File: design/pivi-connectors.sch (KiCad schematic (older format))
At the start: 13 parts, among them P1 Recom_Power_RAC10-05SC/277, P3 CONN_01X05, P4 CONN_01X02, P6 CONN_01X02, P7 CONN_01X05, P8 CONN_01X02, P9 CONN_02X20

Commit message: Moving to PIVI 2.0, added circuits for current clamps
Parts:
- removed P3, P7: CONN_01X05, LESS:CONN-TERM-BLK-5POS-PHOENIX, symbol CONN_01X05
- removed P8: CONN_01X02, LESS:CONN-TERM-BLK-2POS-PHOENIX, symbol CONN_01X02
- added D?: LED_RGB, symbol LED_RGB
- added R? (x3): 270, symbol R
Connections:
- net labels added: CT1_1, CT1_2, CT1_DETECTOR, CT2_1, CT2_2, CT2_DETECTOR, CT3_1, CT3_2, CT3_DETECTOR, CT4_1, CT4_2, CT4_DETECTOR, CT5_1, CT5_2, CT5_DETECTOR, CT6_1, CT6_2, CT6_DETECTOR, GPIO-12, GPIO-18, GPIO-23, GPIO-24, GPIO-25, Neutral_Line, Phase_In
- net labels removed: Neutral1_In, Neutral1_Out, Phase1_In, Phase1_Out, Phase2_In, Phase2_Out, Phase3_In, Phase3_Out, Phase4_In, Phase4_Out, Phase5_In, Phase5_Out, Phase6_In, Phase6_Out
- wire segments 48 -> 72
- no-connect marks 26 -> 21
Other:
- note added: "Audio Jack 3.5 mm female connector\n"
- note added: "Clamp audio connections for SCT-013-000"
- note added: "SJ-3506-SMT"
- note added: "The GPIO pins can draw 50mA safely, distributed\nacross all the pins; an individual GPIO pin can \nonly safely draw 16mA. \n\nhttps://www.raspberrypi.org/documentation/hardw"
- note added: "This connector must meet the following requirements:\n* Internal switch : Avoids noise in pins when the clamp is unplugged.\n* Shielded : Increase endurance, stregth and avoid noise."
- note removed: "277-9761-ND"
- note removed: "Power line output.\nTo load."
- moved on the sheet: C21, D1, JP1, L15, L16, P1, P4, P6, P9, R9

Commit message: Fixing connection errors
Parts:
- gave numbers to parts that had none: 4
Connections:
- net Phase_In renamed Phase_Line
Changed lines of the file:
@@
 Board power Supply Connections
 Text HLabel 7475 5230 2    60   Output ~ 0
-Phase_In
+Phase_Line
 Text HLabel 7475 5330 2    60   Output ~ 0
 Neutral_Line
@@
 GPIO-23
 $Comp
-L LED_RGB D?
+L LED_RGB D2
 U 1 1 55BA51D0
 P 8540 2390
-F 0 "D?" H 8540 2840 50  0000 C CNN
+F 0 "D2" H 8540 2840 50  0000 C CNN
 F 1 "LED_RGB" H 8540 2740 50  0000 C CNN
 F 2 "" H 8540 2340 60  0000 C CNN
@@
 $EndComp
 $Comp
-L R R?
+L R R36
 U 1 1 55BA6452
 P 9040 2190
-F 0 "R?" V 9120 2190 50  0000 C CNN
+F 0 "R36" V 9120 2190 50  0000 C CNN
 F 1 "270" V 9040 2190 50  0000 C CNN
 F 2 "" V 8970 2190 30  0000 C CNN
@@
 $EndComp
 $Comp
-L R R?
+L R R37
 U 1 1 55BA6613
 P 9040 2390
-F 0 "R?" V 9120 2390 50  0000 C CNN
+F 0 "R37" V 9120 2390 50  0000 C CNN
 F 1 "270" V 9040 2390 50  0000 C CNN
 F 2 "" V 8970 2390 30  0000 C CNN
@@
 $EndComp
 $Comp
-L R R?
+L R R38
 U 1 1 55BA674E
 P 9040 2590
-F 0 "R?" V 9120 2590 50  0000 C CNN
+F 0 "R38" V 9120 2590 50  0000 C CNN
 F 1 "270" V 9040 2590 50  0000 C CNN
 F 2 "" V 8970 2590 30  0000 C CNN
@@
 	9440 2190 9440 2915
 $Comp
-L GND #PWR?
+L GND #PWR033
 U 1 1 55BA8447
 P 9440 2915
-F 0 "#PWR?" H 9440 2665 60  0001 C CNN
+F 0 "#PWR033" H 9440 2665 60  0001 C CNN
 F 1 "GND" H 9440 2765 60  0000 C CNN
 F 2 "" H 9440 2915 60  0000 C CNN

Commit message: Agrego los dos circuitos extra para medir tension
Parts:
- D2: footprint (none) -> LEDs:LED_RGB_PLLC-6
- R36, R37, R38: footprint (none) -> Resistors_SMD:R_0603
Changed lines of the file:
@@
 LIBS:memory
 LIBS:xilinx
-LIBS:special
 LIBS:microcontrollers
 LIBS:dsp
@@
 $Descr A4 11693 8268
 encoding utf-8
-Sheet 3 18
+Sheet 3 20
 Title "PIVI"
 Date "Mon 27 Jul 2015"
@@
 F 0 "D2" H 8540 2840 50  0000 C CNN
 F 1 "LED_RGB" H 8540 2740 50  0000 C CNN
-F 2 "" H 8540 2340 60  0000 C CNN
+F 2 "LEDs:LED_RGB_PLLC-6" H 8540 2340 60  0001 C CNN
 F 3 "" H 8540 2340 60  0000 C CNN
 	1    8540 2390
@@
 F 0 "R36" V 9120 2190 50  0000 C CNN
 F 1 "270" V 9040 2190 50  0000 C CNN
-F 2 "" V 8970 2190 30  0000 C CNN
+F 2 "Resistors_SMD:R_0603" V 8970 2190 30  0001 C CNN
 F 3 "" H 9040 2190 30  0000 C CNN
 	1    9040 2190
@@
 F 0 "R37" V 9120 2390 50  0000 C CNN
 F 1 "270" V 9040 2390 50  0000 C CNN
-F 2 "" V 8970 2390 30  0000 C CNN
+F 2 "Resistors_SMD:R_0603" V 8970 2390 30  0001 C CNN
 F 3 "" H 9040 2390 30  0000 C CNN
 	1    9040 2390
@@
 F 0 "R38" V 9120 2590 50  0000 C CNN
 F 1 "270" V 9040 2590 50  0000 C CNN
-F 2 "" V 8970 2590 30  0000 C CNN
+F 2 "Resistors_SMD:R_0603" V 8970 2590 30  0001 C CNN
 F 3 "" H 9040 2590 30  0000 C CNN
 	1    9040 2590

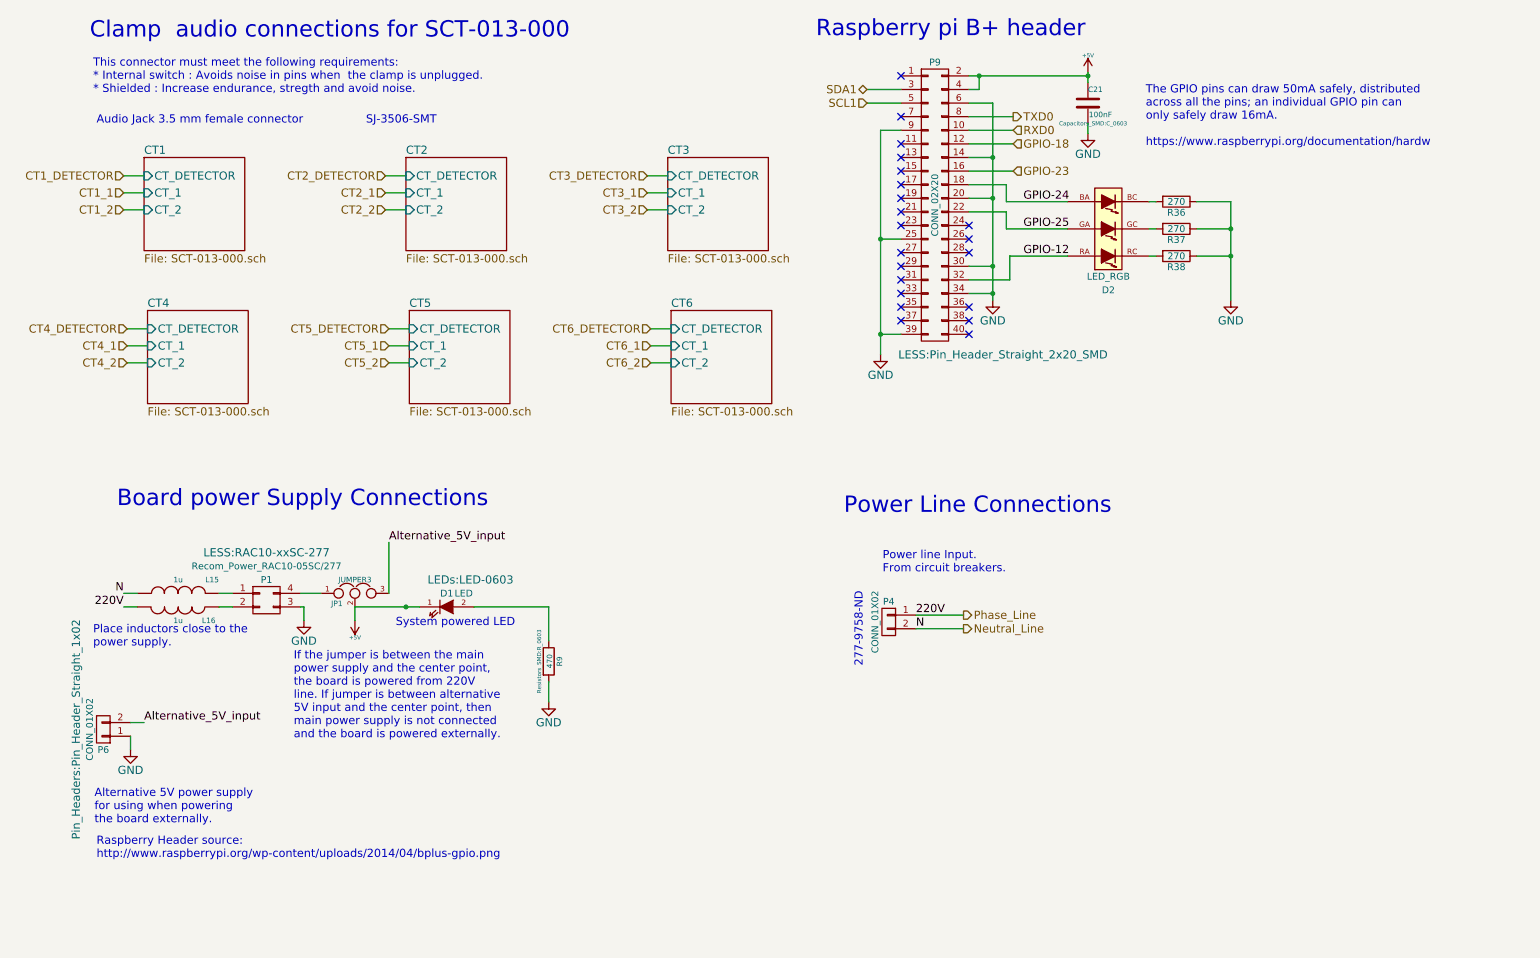
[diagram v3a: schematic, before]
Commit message: Edito conexiones pinza, agregado debub uart, agregado tension referencia
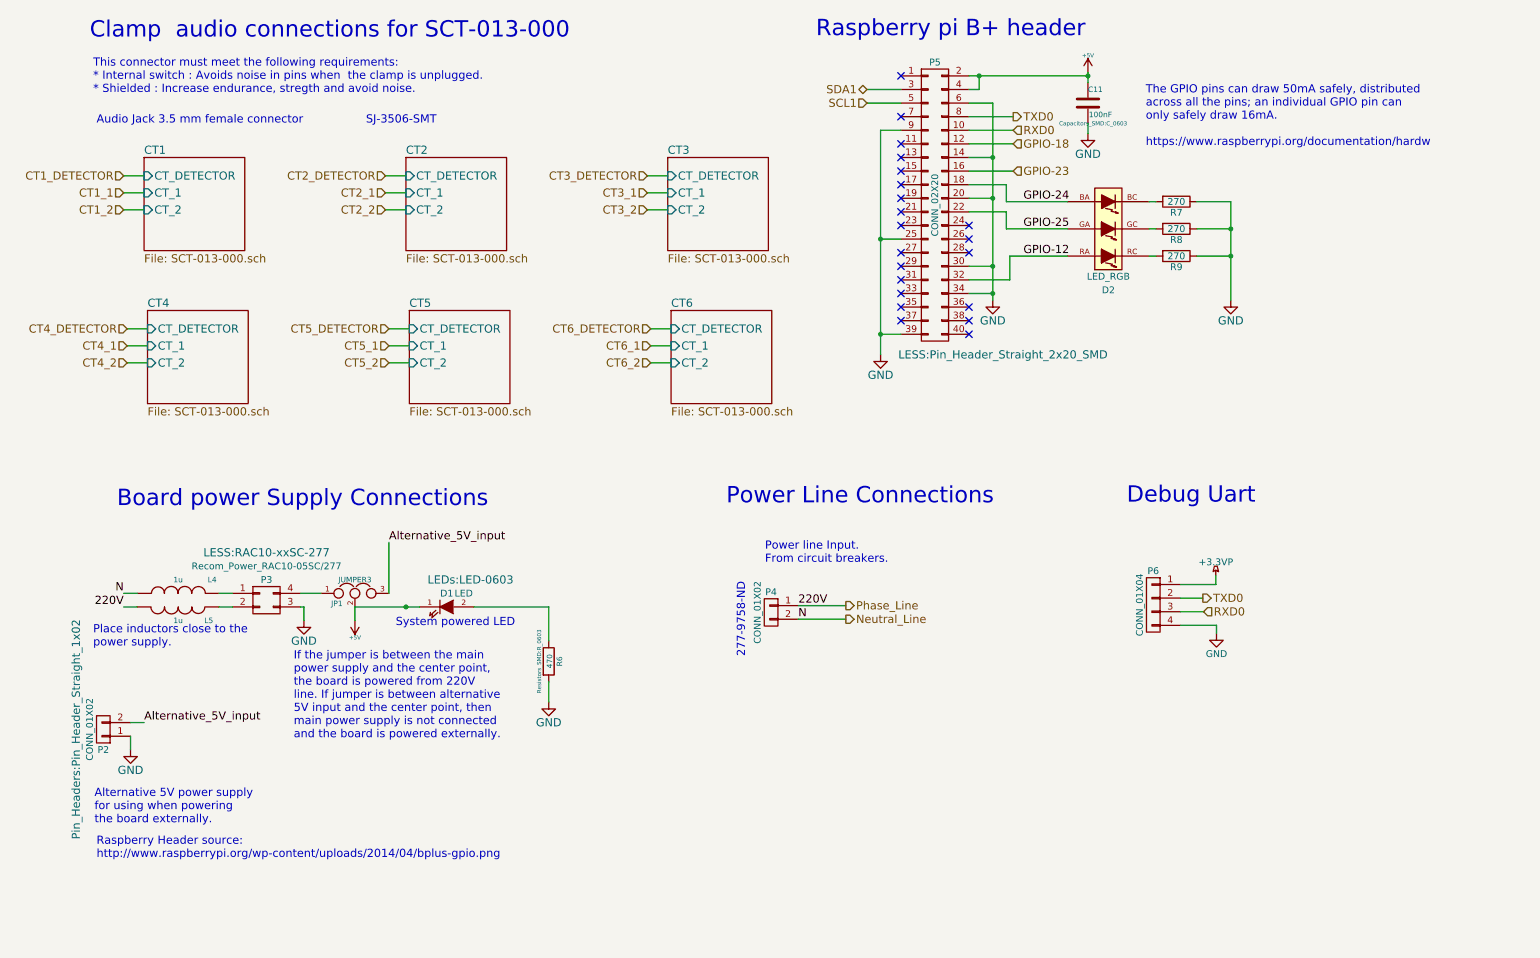
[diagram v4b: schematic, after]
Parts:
- added P6: CONN_01X04, symbol CONN_01X04
- renumbered C21 to C11, L15 to L4, L16 to L5, P6 to P2, P1 to P3, P9 to P5, R9 to R6, R36 to R7, R37 to R8, R38 to R9
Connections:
- net GND: now also P6.4 (P4)
- net RXD0: now also P6.3 (P3)
- net TXD0: now also P6.2 (P2)
- new net +3.3VP: P6.1 (P1)
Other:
- note added: "Debug Uart"
- moved on the sheet: P4
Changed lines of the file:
@@
 $EndDescr
 $Comp
-L +5V #PWR025
+L +5V #PWR27
 U 1 1 54959F0D
 P 8390 1240
-F 0 "#PWR025" H 8390 1330 20  0001 C CNN
+F 0 "#PWR27" H 8390 1330 20  0001 C CNN
 F 1 "+5V" H 8390 1365 30  0000 C CNN
 F 2 "" H 8390 1240 60  0000 C CNN
@@
 $EndComp
 $Comp
-L C C21
+L C C11
 U 1 1 54959F13
 P 8390 1465
-F 0 "C21" H 8390 1565 40  0000 L CNN
+F 0 "C11" H 8390 1565 40  0000 L CNN
 F 1 "100nF" H 8396 1380 40  0000 L CNN
 F 2 "Capacitors_SMD:C_0603" H 8428 1315 30  0000 C CNN
@@
 NoConn ~ 7015 1865
 NoConn ~ 7015 1765
-Text Notes 6880 4925 0    60   ~ 0
+Text Notes 6015 4855 0    60   ~ 0
 Power line Input.\nFrom circuit breakers.
 $Comp
-L +5V #PWR026
+L +5V #PWR23
 U 1 1 54959F4A
 P 3000 5270
-F 0 "#PWR026" H 3000 5360 20  0001 C CNN
+F 0 "#PWR23" H 3000 5360 20  0001 C CNN
 F 1 "+5V" H 3000 5395 30  0000 C CNN
 F 2 "" H 3000 5270 60  0000 C CNN
@@
 	-1   0    0    1
 $EndComp
-Text Notes 6595 4495 0    120  ~ 0
+Text Notes 5730 4425 0    120  ~ 0
 Power Line Connections
 $Comp
-L R R9
+L R R6
 U 1 1 54959F58
 P 4425 5570
-F 0 "R9" V 4505 5570 40  0000 C CNN
+F 0 "R6" V 4505 5570 40  0000 C CNN
 F 1 "470" V 4432 5571 40  0000 C CNN
 F 2 "Resistors_SMD:R_0603" V 4355 5570 30  0000 C CNN
@@
 $EndComp
 $Comp
-L CONN_02X20 P9
+L CONN_02X20 P5
 U 1 1 54959FCF
 P 7265 2215
-F 0 "P9" H 7265 3265 50  0000 C CNN
+F 0 "P5" H 7265 3265 50  0000 C CNN
 F 1 "CONN_02X20" V 7265 2215 50  0000 C CNN
 F 2 "LESS:Pin_Header_Straight_2x20_SMD" H 7765 1115 60  0000 C CNN
@@
 Text Notes 1250 4445 0    120  ~ 0
 Board power Supply Connections
-Text HLabel 7475 5230 2    60   Output ~ 0
+Text HLabel 6610 5160 2    60   Output ~ 0
 Phase_Line
-Text HLabel 7475 5330 2    60   Output ~ 0
+Text HLabel 6610 5260 2    60   Output ~ 0
 Neutral_Line
-Text Label 7125 5230 0    60   ~ 0
+Text Label 6260 5160 0    60   ~ 0
 220V
-Text Label 7125 5330 0    60   ~ 0
+Text Label 6260 5260 0    60   ~ 0
 N
 Text Label 1300 5170 2    60   ~ 0
@@
 RXD0
 $Comp
-L CONN_01X02 P6
+L CONN_01X02 P2
 U 1 1 548F28AD
 P 1150 6070
-F 0 "P6" H 1150 6220 50  0000 C CNN
+F 0 "P2" H 1150 6220 50  0000 C CNN
 F 1 "CONN_01X02" V 1250 6070 50  0000 C CNN
 F 2 "Pin_Headers:Pin_Header_Straight_1x02" V 1350 6070 60  0000 C CNN
@@
 $EndComp
 $Comp
-L INDUCTOR L15
+L INDUCTOR L4
 U 1 1 54C27524
 P 1700 5070
-F 0 "L15" V 1800 4820 40  0000 C CNN
+F 0 "L4" V 1800 4820 40  0000 C CNN
 F 1 "1u" V 1800 5070 40  0000 C CNN
 F 2 "SMD_Packages:SMD-0603" H 1700 5070 60  0001 C CNN
@@
 $EndComp
 $Comp
-L INDUCTOR L16
+L INDUCTOR L5
 U 1 1 54C275D2
 P 1700 5170
-F 0 "L16" V 1800 5395 40  0000 C CNN
+F 0 "L5" V 1800 5395 40  0000 C CNN
 F 1 "1u" V 1800 5170 40  0000 C CNN
 F 2 "SMD_Packages:SMD-0603" H 1700 5170 60  0001 C CNN
@@
 $EndComp
 $Comp
-L GND #PWR027
+L GND #PWR28
 U 1 1 54BFA08A
 P 8390 1690
-F 0 "#PWR027" H 8390 1440 60  0001 C CNN
+F 0 "#PWR28" H 8390 1440 60  0001 C CNN
 F 1 "GND" H 8390 1540 60  0000 C CNN
 F 2 "" H 8390 1690 60  0000 C CNN
@@
 $EndComp
 $Comp
-L GND #PWR028
+L GND #PWR26
 U 1 1 54BFA09E
 P 7690 2915
-F 0 "#PWR028" H 7690 2665 60  0001 C CNN
+F 0 "#PWR26" H 7690 2665 60  0001 C CNN
 F 1 "GND" H 7690 2765 60  0000 C CNN
 F 2 "" H 7690 2915 60  0000 C CNN
@@
 $EndComp
 $Comp
-L GND #PWR029
+L GND #PWR25
 U 1 1 54BFA0B2
 P 6865 3315
-F 0 "#PWR029" H 6865 3065 60  0001 C CNN
+F 0 "#PWR25" H 6865 3065 60  0001 C CNN
 F 1 "GND" H 6865 3165 60  0000 C CNN
 F 2 "" H 6865 3315 60  0000 C CNN
@@
 $EndComp
 $Comp
-L GND #PWR030
+L GND #PWR24
 U 1 1 54BFA0C6
 P 4425 5870
-F 0 "#PWR030" H 4425 5620 60  0001 C CNN
+F 0 "#PWR24" H 4425 5620 60  0001 C CNN
 F 1 "GND" H 4425 5720 60  0000 C CNN
 F 2 "" H 4425 5870 60  0000 C CNN
@@
 $EndComp
 $Comp
-L GND #PWR031
+L GND #PWR22
 U 1 1 54BFA203
 P 2625 5270
-F 0 "#PWR031" H 2625 5020 60  0001 C CNN
+F 0 "#PWR22" H 2625 5020 60  0001 C CNN
 F 1 "GND" H 2625 5120 60  0000 C CNN
 F 2 "" H 2625 5270 60  0000 C CNN
@@
 Alternative 5V power supply \nfor using when powering \nthe board externally.
 $Comp
-L GND #PWR032
+L GND #PWR21
 U 1 1 54C181FB
 P 1350 6220
-F 0 "#PWR032" H 1350 5970 60  0001 C CNN
+F 0 "#PWR21" H 1350 5970 60  0001 C CNN
 F 1 "GND" H 1350 6070 60  0000 C CNN
 F 2 "" H 1350 6220 60  0000 C CNN
@@
 L CONN_01X02 P4
 U 1 1 54C3B67F
-P 6925 5280
-F 0 "P4" H 6925 5430 50  0000 C CNN
-F 1 "CONN_01X02" V 7025 5280 50  0000 C CNN
-F 2 "LESS:CONN-TERM-BLK-2POS-PHOENIX" H 6925 5280 60  0001 C CNN
-F 3 "" H 6925 5280 60  0000 C CNN
-	1    6925 5280
+P 6060 5210
+F 0 "P4" H 6060 5360 50  0000 C CNN
+F 1 "CONN_01X02" V 6160 5210 50  0000 C CNN
+F 2 "LESS:CONN-TERM-BLK-2POS-PHOENIX" H 6060 5210 60  0001 C CNN
+F 3 "" H 6060 5210 60  0000 C CNN
+	1    6060 5210
 	-1   0    0    -1
 $EndComp
 $Comp
-L Recom_Power_RAC10-05SC/277 P1
+L Recom_Power_RAC10-05SC/277 P3
 U 1 1 54C3C5E9
 P 2350 5120
-F 0 "P1" H 2350 5270 50  0000 C CNN
+F 0 "P3" H 2350 5270 50  0000 C CNN
 F 1 "Recom_Power_RAC10-05SC/277" H 2350 5370 50  0000 C CNN
 F 2 "LESS:RAC10-xxSC-277" H 2350 5470 60  0000 C CNN
@@
 	7590 1365 7515 1365
 Wire Wire Line
-	7125 5330 7475 5330
-Wire Wire Line
-	7125 5230 7475 5230
+	6260 5260 6610 5260
+Wire Wire Line
+	6260 5160 6610 5160
 Wire Wire Line
 	2625 5170 2625 5270
@@
 F4 "CT_DETECTOR" I L 1450 2000 60
 $EndSheet
-Text Notes 6740 5610 1    60   ~ 0
+Text Notes 5875 5540 1    60   ~ 0
 277-9758-ND
 Text HLabel 1300 2000 0    60   Input ~ 0
@@
 $EndComp
 $Comp
-L R R36
+L R R7
 U 1 1 55BA6452
 P 9040 2190
-F 0 "R36" V 9120 2190 50  0000 C CNN
+F 0 "R7" V 9120 2190 50  0000 C CNN
 F 1 "270" V 9040 2190 50  0000 C CNN
 F 2 "Resistors_SMD:R_0603" V 8970 2190 30  0001 C CNN
@@
 $EndComp
 $Comp
-L R R37
+L R R8
 U 1 1 55BA6613
 P 9040 2390
-F 0 "R37" V 9120 2390 50  0000 C CNN
+F 0 "R8" V 9120 2390 50  0000 C CNN
 F 1 "270" V 9040 2390 50  0000 C CNN
 F 2 "Resistors_SMD:R_0603" V 8970 2390 30  0001 C CNN
@@
 $EndComp
 $Comp
-L R R38
+L R R9
 U 1 1 55BA674E
 P 9040 2590
-F 0 "R38" V 9120 2590 50  0000 C CNN
+F 0 "R9" V 9120 2590 50  0000 C CNN
 F 1 "270" V 9040 2590 50  0000 C CNN
 F 2 "Resistors_SMD:R_0603" V 8970 2590 30  0001 C CNN
@@
 	9440 2190 9440 2915
 $Comp
-L GND #PWR033
+L GND #PWR31
 U 1 1 55BA8447
 P 9440 2915
-F 0 "#PWR033" H 9440 2665 60  0001 C CNN
+F 0 "#PWR31" H 9440 2665 60  0001 C CNN
 F 1 "GND" H 9440 2765 60  0000 C CNN
 F 2 "" H 9440 2915 60  0000 C CNN
@@
 Text Notes 8815 1790 0    60   ~ 0
 The GPIO pins can draw 50mA safely, distributed\nacross all the pins; an individual GPIO pin can \nonly safely draw 16mA. \n\nhttps://www.raspberrypi.org/documentation/hardw
+Text Notes 8675 4420 0    120  ~ 0
+Debug Uart
+$Comp
+L CONN_01X04 P6
+U 1 1 55BE90A6
+P 8870 5155
+F 0 "P6" H 8870 5405 50  0000 C CNN
+F 1 "CONN_01X04" V 8970 5155 50  0000 C CNN
+F 2 "" H 8870 5155 60  0000 C CNN
+F 3 "" H 8870 5155 60  0000 C CNN
+	1    8870 5155
+	-1   0    0    -1
+$EndComp
+$Comp
+L +3.3VP #PWR29
+U 1 1 55BEAB18
+P 9330 4940
+F 0 "#PWR29" H 9480 4890 50  0001 C CNN
+F 1 "+3.3VP" H 9330 5040 50  0000 C CNN
+F 2 "" H 9330 4940 60  0000 C CNN
+F 3 "" H 9330 4940 60  0000 C CNN
+	1    9330 4940
+	1    0    0    -1
+$EndComp
+Wire Wire Line
+	9070 5005 9330 5005
+Wire Wire Line
+	9330 5005 9330 4940
+Wire Wire Line
+	9070 5305 9335 5305
+Wire Wire Line
+	9335 5305 9335 5365
+$Comp
+L GND #PWR30
+U 1 1 55BEFFD5
+P 9335 5365
+F 0 "#PWR30" H 9335 5115 50  0001 C CNN
+F 1 "GND" H 9335 5215 50  0000 C CNN
+F 2 "" H 9335 5365 60  0000 C CNN
+F 3 "" H 9335 5365 60  0000 C CNN
+	1    9335 5365
+	1    0    0    -1
+$EndComp
+Text HLabel 9235 5105 2    60   Output ~ 0
+TXD0
+Text HLabel 9240 5205 2    60   Input ~ 0
+RXD0
+Wire Wire Line
+	9070 5105 9235 5105
+Wire Wire Line
+	9070 5205 9240 5205
 $EndSCHEMATC
